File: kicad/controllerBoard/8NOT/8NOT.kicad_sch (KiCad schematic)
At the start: 16 parts

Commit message: demux
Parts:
- renumbered Q to Q101, Q to Q102, Q to Q108, Q to Q112, Q to Q59, Q to Q60, Q to Q66, Q to Q70, Q to Q73, Q to Q74, Q to Q80, Q to Q84, Q to Q87, Q to Q88, Q to Q94, Q to Q98
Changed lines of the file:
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@@
 		(dnp no)
 		(fields_autoplaced yes)
-		(property "Reference" "Q"
+		(property "Reference" "Q70"
 			(at 93.98 77.4699 0)
 			(show_name no)
@@
 			(project "controllerBoard"
 				(path "/93a9a1ca-4ee5-40da-ab67-92836146c003/4d7a1886-fab4-478f-9237-fb2bf1fb5a44"
+					(reference "Q70")
+					(unit 1)
+				)
+				(path "/93a9a1ca-4ee5-40da-ab67-92836146c003/c2b4eaa1-1e50-43e7-b958-b128cd60509e"
 					(reference "Q70")
 					(unit 1)
@@
 		(dnp no)
 		(fields_autoplaced yes)
-		(property "Reference" "Q"
+		(property "Reference" "Q80"
 			(at 129.54 67.3099 0)
 			(show_name no)
@@
 			(project "controllerBoard"
 				(path "/93a9a1ca-4ee5-40da-ab67-92836146c003/4d7a1886-fab4-478f-9237-fb2bf1fb5a44"
+					(reference "Q80")
+					(unit 1)
+				)
+				(path "/93a9a1ca-4ee5-40da-ab67-92836146c003/c2b4eaa1-1e50-43e7-b958-b128cd60509e"
 					(reference "Q80")
 					(unit 1)
@@
 		(dnp no)
 		(fields_autoplaced yes)
-		(property "Reference" "Q"
+		(property "Reference" "Q94"
 			(at 165.1 67.3099 0)
 			(show_name no)
@@
 			(project "controllerBoard"
 				(path "/93a9a1ca-4ee5-40da-ab67-92836146c003/4d7a1886-fab4-478f-9237-fb2bf1fb5a44"
+					(reference "Q94")
+					(unit 1)
+				)
+				(path "/93a9a1ca-4ee5-40da-ab67-92836146c003/c2b4eaa1-1e50-43e7-b958-b128cd60509e"
 					(reference "Q94")
 					(unit 1)
@@
 		(dnp no)
 		(fields_autoplaced yes)
-		(property "Reference" "#PWR"
+		(property "Reference" "#PWR052"
 			(at 133.35 60.96 0)
 			(hide yes)
@@
 			(project "controllerBoard"
 				(path "/93a9a1ca-4ee5-40da-ab67-92836146c003/4d7a1886-fab4-478f-9237-fb2bf1fb5a44"
+					(reference "#PWR052")
+					(unit 1)
+				)
+				(path "/93a9a1ca-4ee5-40da-ab67-92836146c003/c2b4eaa1-1e50-43e7-b958-b128cd60509e"
 					(reference "#PWR052")
 					(unit 1)
@@
 		(dnp no)
 		(fields_autoplaced yes)
-		(property "Reference" "Q"
+		(property "Reference" "Q101"
 			(at 182.88 67.3099 0)
 			(show_name no)
@@
 			(project "controllerBoard"
 				(path "/93a9a1ca-4ee5-40da-ab67-92836146c003/4d7a1886-fab4-478f-9237-fb2bf1fb5a44"
+					(reference "Q101")
+					(unit 1)
+				)
+				(path "/93a9a1ca-4ee5-40da-ab67-92836146c003/c2b4eaa1-1e50-43e7-b958-b128cd60509e"
 					(reference "Q101")
 					(unit 1)
@@
 		(dnp no)
 		(fields_autoplaced yes)
-		(property "Reference" "Q"
+		(property "Reference" "Q59"
 			(at 76.2 67.3099 0)
 			(show_name no)
@@
 			(project "controllerBoard"
 				(path "/93a9a1ca-4ee5-40da-ab67-92836146c003/4d7a1886-fab4-478f-9237-fb2bf1fb5a44"
+					(reference "Q59")
+					(unit 1)
+				)
+				(path "/93a9a1ca-4ee5-40da-ab67-92836146c003/c2b4eaa1-1e50-43e7-b958-b128cd60509e"
 					(reference "Q59")
 					(unit 1)
@@
 		(dnp no)
 		(fields_autoplaced yes)
-		(property "Reference" "Q"
+		(property "Reference" "Q98"
 			(at 165.1 77.4699 0)
 			(show_name no)
@@
 			(project "controllerBoard"
 				(path "/93a9a1ca-4ee5-40da-ab67-92836146c003/4d7a1886-fab4-478f-9237-fb2bf1fb5a44"
+					(reference "Q98")
+					(unit 1)
+				)
+				(path "/93a9a1ca-4ee5-40da-ab67-92836146c003/c2b4eaa1-1e50-43e7-b958-b128cd60509e"
 					(reference "Q98")
 					(unit 1)
@@
 		(dnp no)
 		(fields_autoplaced yes)
-		(property "Reference" "Q"
+		(property "Reference" "Q60"
 			(at 76.2 77.4699 0)
 			(show_name no)
@@
 			(project "controllerBoard"
 				(path "/93a9a1ca-4ee5-40da-ab67-92836146c003/4d7a1886-fab4-478f-9237-fb2bf1fb5a44"
+					(reference "Q60")
+					(unit 1)
+				)
+				(path "/93a9a1ca-4ee5-40da-ab67-92836146c003/c2b4eaa1-1e50-43e7-b958-b128cd60509e"
 					(reference "Q60")
 					(unit 1)
@@
 		(dnp no)
 		(fields_autoplaced yes)
-		(property "Reference" "Q"
+		(property "Reference" "Q108"
 			(at 200.66 67.3099 0)
 			(show_name no)
@@
 			(project "controllerBoard"
 				(path "/93a9a1ca-4ee5-40da-ab67-92836146c003/4d7a1886-fab4-478f-9237-fb2bf1fb5a44"
+					(reference "Q108")
+					(unit 1)
+				)
+				(path "/93a9a1ca-4ee5-40da-ab67-92836146c003/c2b4eaa1-1e50-43e7-b958-b128cd60509e"
 					(reference "Q108")
 					(unit 1)
@@
 		(dnp no)
 		(fields_autoplaced yes)
-		(property "Reference" "Q"
+		(property "Reference" "Q102"
 			(at 182.88 77.4699 0)
 			(show_name no)
@@
 			(project "controllerBoard"
 				(path "/93a9a1ca-4ee5-40da-ab67-92836146c003/4d7a1886-fab4-478f-9237-fb2bf1fb5a44"
+					(reference "Q102")
+					(unit 1)
+				)
+				(path "/93a9a1ca-4ee5-40da-ab67-92836146c003/c2b4eaa1-1e50-43e7-b958-b128cd60509e"
 					(reference "Q102")
 					(unit 1)
@@
 		(dnp no)
 		(fields_autoplaced yes)
-		(property "Reference" "Q"
+		(property "Reference" "Q112"
 			(at 200.66 77.4699 0)
 			(show_name no)
@@
 			(project "controllerBoard"
 				(path "/93a9a1ca-4ee5-40da-ab67-92836146c003/4d7a1886-fab4-478f-9237-fb2bf1fb5a44"
+					(reference "Q112")
+					(unit 1)
+				)
+				(path "/93a9a1ca-4ee5-40da-ab67-92836146c003/c2b4eaa1-1e50-43e7-b958-b128cd60509e"
 					(reference "Q112")
 					(unit 1)
@@
 		(dnp no)
 		(fields_autoplaced yes)
-		(property "Reference" "#PWR"
+		(property "Reference" "#PWR053"
 			(at 133.35 96.52 0)
 			(hide yes)
@@
 			(project "controllerBoard"
 				(path "/93a9a1ca-4ee5-40da-ab67-92836146c003/4d7a1886-fab4-478f-9237-fb2bf1fb5a44"
+					(reference "#PWR053")
+					(unit 1)
+				)
+				(path "/93a9a1ca-4ee5-40da-ab67-92836146c003/c2b4eaa1-1e50-43e7-b958-b128cd60509e"
 					(reference "#PWR053")
 					(unit 1)
@@
 		(dnp no)
 		(fields_autoplaced yes)
-		(property "Reference" "Q"
+		(property "Reference" "Q74"
 			(at 111.76 77.4699 0)
 			(show_name no)
@@
 			(project "controllerBoard"
 				(path "/93a9a1ca-4ee5-40da-ab67-92836146c003/4d7a1886-fab4-478f-9237-fb2bf1fb5a44"
+					(reference "Q74")
+					(unit 1)
+				)
+				(path "/93a9a1ca-4ee5-40da-ab67-92836146c003/c2b4eaa1-1e50-43e7-b958-b128cd60509e"
 					(reference "Q74")
 					(unit 1)
@@
 		(dnp no)
 		(fields_autoplaced yes)
-		(property "Reference" "Q"
+		(property "Reference" "Q73"
 			(at 111.76 67.3099 0)
 			(show_name no)
@@
 			(project "controllerBoard"
 				(path "/93a9a1ca-4ee5-40da-ab67-92836146c003/4d7a1886-fab4-478f-9237-fb2bf1fb5a44"
+					(reference "Q73")
+					(unit 1)
+				)
+				(path "/93a9a1ca-4ee5-40da-ab67-92836146c003/c2b4eaa1-1e50-43e7-b958-b128cd60509e"
 					(reference "Q73")
 					(unit 1)
@@
 		(dnp no)
 		(fields_autoplaced yes)
-		(property "Reference" "Q"
+		(property "Reference" "Q66"
 			(at 93.98 67.3099 0)
 			(show_name no)
@@
 			(project "controllerBoard"
 				(path "/93a9a1ca-4ee5-40da-ab67-92836146c003/4d7a1886-fab4-478f-9237-fb2bf1fb5a44"
+					(reference "Q66")
+					(unit 1)
+				)
+				(path "/93a9a1ca-4ee5-40da-ab67-92836146c003/c2b4eaa1-1e50-43e7-b958-b128cd60509e"
 					(reference "Q66")
 					(unit 1)
@@
 		(dnp no)
 		(fields_autoplaced yes)
-		(property "Reference" "Q"
+		(property "Reference" "Q88"
 			(at 147.32 77.4699 0)
 			(show_name no)
@@
 			(project "controllerBoard"
 				(path "/93a9a1ca-4ee5-40da-ab67-92836146c003/4d7a1886-fab4-478f-9237-fb2bf1fb5a44"
+					(reference "Q88")
+					(unit 1)
+				)
+				(path "/93a9a1ca-4ee5-40da-ab67-92836146c003/c2b4eaa1-1e50-43e7-b958-b128cd60509e"
 					(reference "Q88")
 					(unit 1)
@@
 		(dnp no)
 		(fields_autoplaced yes)
-		(property "Reference" "Q"
+		(property "Reference" "Q84"
 			(at 129.54 77.4699 0)
 			(show_name no)
@@
 			(project "controllerBoard"
 				(path "/93a9a1ca-4ee5-40da-ab67-92836146c003/4d7a1886-fab4-478f-9237-fb2bf1fb5a44"
+					(reference "Q84")
+					(unit 1)
+				)
+				(path "/93a9a1ca-4ee5-40da-ab67-92836146c003/c2b4eaa1-1e50-43e7-b958-b128cd60509e"
 					(reference "Q84")
 					(unit 1)
@@
 		(dnp no)
 		(fields_autoplaced yes)
-		(property "Reference" "Q"
+		(property "Reference" "Q87"
 			(at 147.32 67.3099 0)
 			(show_name no)
@@
 					(reference "Q87")
 					(unit 1)
+				)
+				(path "/93a9a1ca-4ee5-40da-ab67-92836146c003/c2b4eaa1-1e50-43e7-b958-b128cd60509e"
+					(reference "Q87")
+					(unit 1)

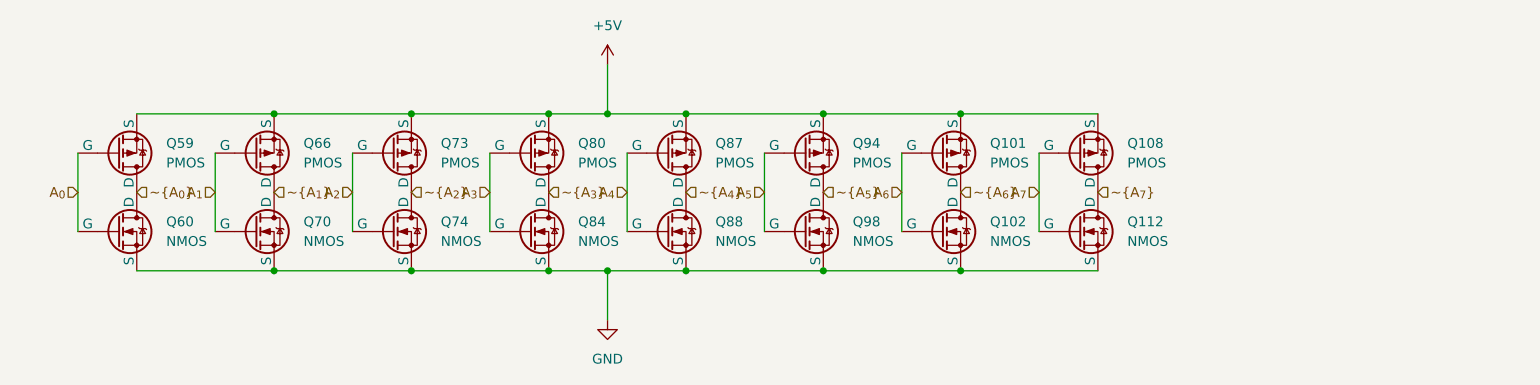
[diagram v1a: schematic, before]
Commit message: update main board schematic
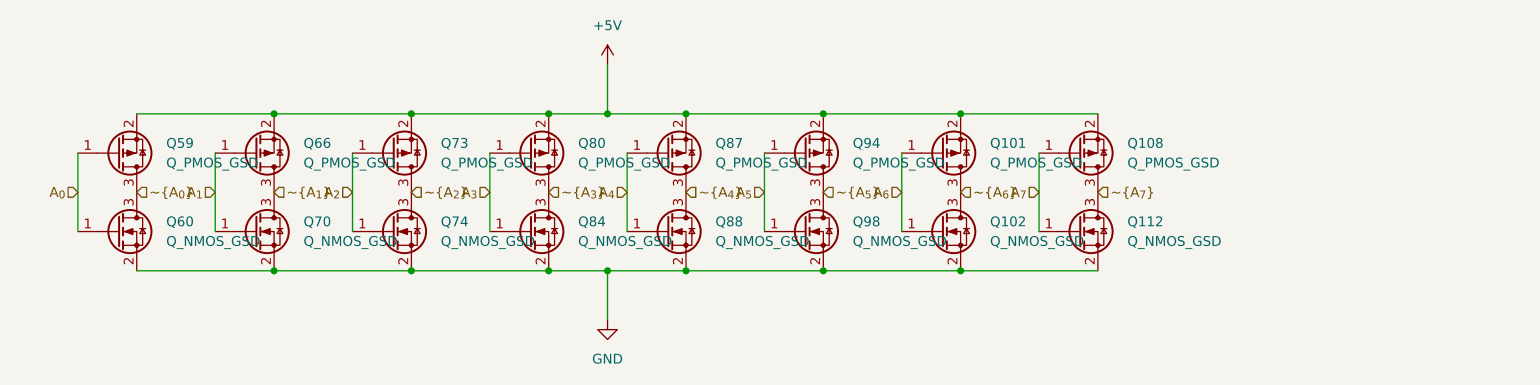
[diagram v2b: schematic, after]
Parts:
- Q101, Q108, Q59, Q66, Q73, Q80, Q87, Q94: value PMOS -> Q_PMOS_GSD; symbol Simulation_SPICE:PMOS -> Transistor_FET:Q_PMOS_GSD
- Q102, Q112, Q60, Q70, Q74, Q84, Q88, Q98: value NMOS -> Q_NMOS_GSD; symbol Simulation_SPICE:NMOS -> Transistor_FET:Q_NMOS_GSD
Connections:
- net +5V: now also Q101.2 (S), Q108.2 (S), Q59.2 (S), Q66.2 (S), Q73.2 (S), Q80.2 (S), Q87.2 (S), Q94.2 (S); no longer Q101.3 (S), Q108.3 (S), Q59.3 (S), Q66.3 (S), Q73.3 (S), Q80.3 (S), Q87.3 (S), Q94.3 (S)
- net A_{0}: now also Q59.1 (G), Q60.1 (G); no longer Q59.2 (G), Q60.2 (G)
- net A_{1}: now also Q66.1 (G), Q70.1 (G); no longer Q66.2 (G), Q70.2 (G)
- net A_{2}: now also Q73.1 (G), Q74.1 (G); no longer Q73.2 (G), Q74.2 (G)
- net A_{3}: now also Q80.1 (G), Q84.1 (G); no longer Q80.2 (G), Q84.2 (G)
- net A_{4}: now also Q87.1 (G), Q88.1 (G); no longer Q87.2 (G), Q88.2 (G)
- net A_{5}: now also Q94.1 (G), Q98.1 (G); no longer Q94.2 (G), Q98.2 (G)
- net A_{6}: now also Q101.1 (G), Q102.1 (G); no longer Q101.2 (G), Q102.2 (G)
- net A_{7}: now also Q108.1 (G), Q112.1 (G); no longer Q108.2 (G), Q112.2 (G)
- net GND: now also Q102.2 (S), Q112.2 (S), Q60.2 (S), Q70.2 (S), Q74.2 (S), Q84.2 (S), Q88.2 (S), Q98.2 (S); no longer Q102.3 (S), Q112.3 (S), Q60.3 (S), Q70.3 (S), Q74.3 (S), Q84.3 (S), Q88.3 (S), Q98.3 (S)
- net ~{A_{0}}: now also Q59.3 (D), Q60.3 (D); no longer Q59.1 (D), Q60.1 (D)
- net ~{A_{1}}: now also Q66.3 (D), Q70.3 (D); no longer Q66.1 (D), Q70.1 (D)
- net ~{A_{2}}: now also Q73.3 (D), Q74.3 (D); no longer Q73.1 (D), Q74.1 (D)
- net ~{A_{3}}: now also Q80.3 (D), Q84.3 (D); no longer Q80.1 (D), Q84.1 (D)
- net ~{A_{4}}: now also Q87.3 (D), Q88.3 (D); no longer Q87.1 (D), Q88.1 (D)
- net ~{A_{5}}: now also Q94.3 (D), Q98.3 (D); no longer Q94.1 (D), Q98.1 (D)
- net ~{A_{6}}: now also Q101.3 (D), Q102.3 (D); no longer Q101.1 (D), Q102.1 (D)
- net ~{A_{7}}: now also Q108.3 (D), Q112.3 (D); no longer Q108.1 (D), Q112.1 (D)
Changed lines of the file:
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@@
 	)
 	(symbol
-		(lib_id "Simulation_SPICE:NMOS")
+		(lib_id "Transistor_FET:Q_NMOS_GSD")
 		(at 87.63 78.74 0)
 		(unit 1)
@@
 			)
 		)
-		(property "Value" "NMOS"
+		(property "Value" "Q_NMOS_GSD"
 			(at 93.98 80.0099 0)
 			(show_name no)
@@
 		)
 		(instances
+			(project "8NOT"
+				(path "/14128147-f14f-486f-9b79-b3c9d1046bb8"
+					(reference "Q70")
+					(unit 1)
+				)
+			)
 			(project "controllerBoard"
 				(path "/93a9a1ca-4ee5-40da-ab67-92836146c003/4d7a1886-fab4-478f-9237-fb2bf1fb5a44"
@@
 	)
 	(symbol
-		(lib_id "Simulation_SPICE:PMOS")
+		(lib_id "Transistor_FET:Q_PMOS_GSD")
 		(at 123.19 68.58 0)
 		(mirror x)
@@
 			)
 		)
-		(property "Value" "PMOS"
+		(property "Value" "Q_PMOS_GSD"
 			(at 129.54 69.8499 0)
 			(show_name no)
@@
 		)
 		(instances
+			(project "8NOT"
+				(path "/14128147-f14f-486f-9b79-b3c9d1046bb8"
+					(reference "Q80")
+					(unit 1)
+				)
+			)
 			(project "controllerBoard"
 				(path "/93a9a1ca-4ee5-40da-ab67-92836146c003/4d7a1886-fab4-478f-9237-fb2bf1fb5a44"
@@
 	)
 	(symbol
-		(lib_id "Simulation_SPICE:PMOS")
+		(lib_id "Transistor_FET:Q_PMOS_GSD")
 		(at 158.75 68.58 0)
 		(mirror x)
@@
 			)
 		)
-		(property "Value" "PMOS"
+		(property "Value" "Q_PMOS_GSD"
 			(at 165.1 69.8499 0)
 			(show_name no)
@@
 		)
 		(instances
+			(project "8NOT"
+				(path "/14128147-f14f-486f-9b79-b3c9d1046bb8"
+					(reference "Q94")
+					(unit 1)
+				)
+			)
 			(project "controllerBoard"
 				(path "/93a9a1ca-4ee5-40da-ab67-92836146c003/4d7a1886-fab4-478f-9237-fb2bf1fb5a44"
@@
 		)
 		(instances
+			(project "8NOT"
+				(path "/14128147-f14f-486f-9b79-b3c9d1046bb8"
+					(reference "#PWR052")
+					(unit 1)
+				)
+			)
 			(project "controllerBoard"
 				(path "/93a9a1ca-4ee5-40da-ab67-92836146c003/4d7a1886-fab4-478f-9237-fb2bf1fb5a44"
@@
 	)
 	(symbol
-		(lib_id "Simulation_SPICE:PMOS")
+		(lib_id "Transistor_FET:Q_PMOS_GSD")
 		(at 176.53 68.58 0)
 		(mirror x)
@@
 			)
 		)
-		(property "Value" "PMOS"
+		(property "Value" "Q_PMOS_GSD"
 			(at 182.88 69.8499 0)
 			(show_name no)
@@
 		)
 		(instances
+			(project "8NOT"
+				(path "/14128147-f14f-486f-9b79-b3c9d1046bb8"
+					(reference "Q101")
+					(unit 1)
+				)
+			)
 			(project "controllerBoard"
 				(path "/93a9a1ca-4ee5-40da-ab67-92836146c003/4d7a1886-fab4-478f-9237-fb2bf1fb5a44"
@@
 	)
 	(symbol
-		(lib_id "Simulation_SPICE:PMOS")
+		(lib_id "Transistor_FET:Q_PMOS_GSD")
 		(at 69.85 68.58 0)
 		(mirror x)
@@
 			)
 		)
-		(property "Value" "PMOS"
+		(property "Value" "Q_PMOS_GSD"
 			(at 76.2 69.8499 0)
 			(show_name no)
@@
 		)
 		(instances
+			(project "8NOT"
+				(path "/14128147-f14f-486f-9b79-b3c9d1046bb8"
+					(reference "Q59")
+					(unit 1)
+				)
+			)
 			(project "controllerBoard"
 				(path "/93a9a1ca-4ee5-40da-ab67-92836146c003/4d7a1886-fab4-478f-9237-fb2bf1fb5a44"
@@
 	)
 	(symbol
-		(lib_id "Simulation_SPICE:NMOS")
+		(lib_id "Transistor_FET:Q_NMOS_GSD")
 		(at 158.75 78.74 0)
 		(unit 1)
@@
 			)
 		)
-		(property "Value" "NMOS"
+		(property "Value" "Q_NMOS_GSD"
 			(at 165.1 80.0099 0)
 			(show_name no)
@@
 		)
 		(instances
+			(project "8NOT"
+				(path "/14128147-f14f-486f-9b79-b3c9d1046bb8"
+					(reference "Q98")
+					(unit 1)
+				)
+			)
 			(project "controllerBoard"
 				(path "/93a9a1ca-4ee5-40da-ab67-92836146c003/4d7a1886-fab4-478f-9237-fb2bf1fb5a44"
@@
 	)
 	(symbol
-		(lib_id "Simulation_SPICE:NMOS")
+		(lib_id "Transistor_FET:Q_NMOS_GSD")
 		(at 69.85 78.74 0)
 		(unit 1)
@@
 			)
 		)
-		(property "Value" "NMOS"
+		(property "Value" "Q_NMOS_GSD"
 			(at 76.2 80.0099 0)
 			(show_name no)
@@
 		)
 		(instances
+			(project "8NOT"
+				(path "/14128147-f14f-486f-9b79-b3c9d1046bb8"
+					(reference "Q60")
+					(unit 1)
+				)
+			)
 			(project "controllerBoard"
 				(path "/93a9a1ca-4ee5-40da-ab67-92836146c003/4d7a1886-fab4-478f-9237-fb2bf1fb5a44"
@@
 	)
 	(symbol
-		(lib_id "Simulation_SPICE:PMOS")
+		(lib_id "Transistor_FET:Q_PMOS_GSD")
 		(at 194.31 68.58 0)
 		(mirror x)
@@
 			)
 		)
-		(property "Value" "PMOS"
+		(property "Value" "Q_PMOS_GSD"
 			(at 200.66 69.8499 0)
 			(show_name no)
@@
 		)
 		(instances
+			(project "8NOT"
+				(path "/14128147-f14f-486f-9b79-b3c9d1046bb8"
+					(reference "Q108")
+					(unit 1)
+				)
+			)
 			(project "controllerBoard"
 				(path "/93a9a1ca-4ee5-40da-ab67-92836146c003/4d7a1886-fab4-478f-9237-fb2bf1fb5a44"
@@
 	)
 	(symbol
-		(lib_id "Simulation_SPICE:NMOS")
+		(lib_id "Transistor_FET:Q_NMOS_GSD")
 		(at 176.53 78.74 0)
 		(unit 1)
@@
 			)
 		)
-		(property "Value" "NMOS"
+		(property "Value" "Q_NMOS_GSD"
 			(at 182.88 80.0099 0)
 			(show_name no)
@@
 		)
 		(instances
+			(project "8NOT"
+				(path "/14128147-f14f-486f-9b79-b3c9d1046bb8"
+					(reference "Q102")
+					(unit 1)
+				)
+			)
 			(project "controllerBoard"
 				(path "/93a9a1ca-4ee5-40da-ab67-92836146c003/4d7a1886-fab4-478f-9237-fb2bf1fb5a44"
@@
 	)
 	(symbol
-		(lib_id "Simulation_SPICE:NMOS")
+		(lib_id "Transistor_FET:Q_NMOS_GSD")
 		(at 194.31 78.74 0)
 		(unit 1)
@@
 			)
 		)
-		(property "Value" "NMOS"
+		(property "Value" "Q_NMOS_GSD"
 			(at 200.66 80.0099 0)
 			(show_name no)
@@
 		)
 		(instances
+			(project "8NOT"
+				(path "/14128147-f14f-486f-9b79-b3c9d1046bb8"
+					(reference "Q112")
+					(unit 1)
+				)
+			)
 			(project "controllerBoard"
 				(path "/93a9a1ca-4ee5-40da-ab67-92836146c003/4d7a1886-fab4-478f-9237-fb2bf1fb5a44"
@@
 		)
 		(instances
+			(project "8NOT"
+				(path "/14128147-f14f-486f-9b79-b3c9d1046bb8"
+					(reference "#PWR053")
+					(unit 1)
+				)
+			)
 			(project "controllerBoard"
 				(path "/93a9a1ca-4ee5-40da-ab67-92836146c003/4d7a1886-fab4-478f-9237-fb2bf1fb5a44"
@@
 	)
 	(symbol
-		(lib_id "Simulation_SPICE:NMOS")
+		(lib_id "Transistor_FET:Q_NMOS_GSD")
 		(at 105.41 78.74 0)
 		(unit 1)
@@
 			)
 		)
-		(property "Value" "NMOS"
+		(property "Value" "Q_NMOS_GSD"
 			(at 111.76 80.0099 0)
 			(show_name no)
@@
 		)
 		(instances
+			(project "8NOT"
+				(path "/14128147-f14f-486f-9b79-b3c9d1046bb8"
+					(reference "Q74")
+					(unit 1)
+				)
+			)
 			(project "controllerBoard"
 				(path "/93a9a1ca-4ee5-40da-ab67-92836146c003/4d7a1886-fab4-478f-9237-fb2bf1fb5a44"
@@
 	)
 	(symbol
-		(lib_id "Simulation_SPICE:PMOS")
+		(lib_id "Transistor_FET:Q_PMOS_GSD")
 		(at 105.41 68.58 0)
 		(mirror x)
@@
 			)
 		)
-		(property "Value" "PMOS"
+		(property "Value" "Q_PMOS_GSD"
 			(at 111.76 69.8499 0)
 			(show_name no)
@@
 		)
 		(instances
+			(project "8NOT"
+				(path "/14128147-f14f-486f-9b79-b3c9d1046bb8"
+					(reference "Q73")
+					(unit 1)
+				)
+			)
 			(project "controllerBoard"
 				(path "/93a9a1ca-4ee5-40da-ab67-92836146c003/4d7a1886-fab4-478f-9237-fb2bf1fb5a44"
@@
 	)
 	(symbol
-		(lib_id "Simulation_SPICE:PMOS")
+		(lib_id "Transistor_FET:Q_PMOS_GSD")
 		(at 87.63 68.58 0)
 		(mirror x)
@@
 			)
 		)
-		(property "Value" "PMOS"
+		(property "Value" "Q_PMOS_GSD"
 			(at 93.98 69.8499 0)
 			(show_name no)
@@
 		)
 		(instances
+			(project "8NOT"
+				(path "/14128147-f14f-486f-9b79-b3c9d1046bb8"
+					(reference "Q66")
+					(unit 1)
+				)
+			)
 			(project "controllerBoard"
 				(path "/93a9a1ca-4ee5-40da-ab67-92836146c003/4d7a1886-fab4-478f-9237-fb2bf1fb5a44"
@@
 	)
 	(symbol
-		(lib_id "Simulation_SPICE:NMOS")
+		(lib_id "Transistor_FET:Q_NMOS_GSD")
 		(at 140.97 78.74 0)
 		(unit 1)
@@
 			)
 		)
-		(property "Value" "NMOS"
+		(property "Value" "Q_NMOS_GSD"
 			(at 147.32 80.0099 0)
 			(show_name no)
@@
 		)
 		(instances
+			(project "8NOT"
+				(path "/14128147-f14f-486f-9b79-b3c9d1046bb8"
+					(reference "Q88")
+					(unit 1)
+				)
+			)
 			(project "controllerBoard"
 				(path "/93a9a1ca-4ee5-40da-ab67-92836146c003/4d7a1886-fab4-478f-9237-fb2bf1fb5a44"
@@
 	)
 	(symbol
-		(lib_id "Simulation_SPICE:NMOS")
+		(lib_id "Transistor_FET:Q_NMOS_GSD")
 		(at 123.19 78.74 0)
 		(unit 1)
@@
 			)
 		)
-		(property "Value" "NMOS"
+		(property "Value" "Q_NMOS_GSD"
 			(at 129.54 80.0099 0)
 			(show_name no)
@@
 		)
 		(instances
+			(project "8NOT"
+				(path "/14128147-f14f-486f-9b79-b3c9d1046bb8"
+					(reference "Q84")
+					(unit 1)
+				)
+			)
 			(project "controllerBoard"
 				(path "/93a9a1ca-4ee5-40da-ab67-92836146c003/4d7a1886-fab4-478f-9237-fb2bf1fb5a44"
@@
 	)
 	(symbol
-		(lib_id "Simulation_SPICE:PMOS")
+		(lib_id "Transistor_FET:Q_PMOS_GSD")
 		(at 140.97 68.58 0)
 		(mirror x)
@@
 			)
 		)
-		(property "Value" "PMOS"
+		(property "Value" "Q_PMOS_GSD"
 			(at 147.32 69.8499 0)
 			(show_name no)
@@
 		)
 		(instances
+			(project "8NOT"
+				(path "/14128147-f14f-486f-9b79-b3c9d1046bb8"
+					(reference "Q87")
+					(unit 1)
+				)
+			)
 			(project "controllerBoard"
 				(path "/93a9a1ca-4ee5-40da-ab67-92836146c003/4d7a1886-fab4-478f-9237-fb2bf1fb5a44"
@@
 		)
 	)
+	(sheet_instances
+		(path "/"
+			(page "1")
+		)
+	)
+	(embedded_fonts no)
 )

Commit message: finished routing all sub schematics
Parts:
- added C1, C2, C3, C4: C, Capacitor_SMD:C_0805_2012Metric_Pad1.18x1.45mm_HandSolder, symbol Device:C
- Q101, Q108, Q59, Q66, Q73, Q80, Q87, Q94: footprint (none) -> easyeda2kicad:SOT-23-P
- Q102, Q112, Q60, Q70, Q74, Q84, Q88, Q98: footprint (none) -> easyeda2kicad:SOT-23-N
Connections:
- net +5V: now also C1.1, C2.1, C3.1, C4.1
- net GND: now also C1.2, C2.2, C3.2, C4.2
